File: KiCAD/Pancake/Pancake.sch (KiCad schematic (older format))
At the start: 12 parts, among them J1 Conn_01x08_Male, J2 Conn_01x08_Male, J3 Conn_01x08_Male, J4 Conn_01x10_Male, J5 Conn_01x08_Male, J6 Conn_01x08_Male

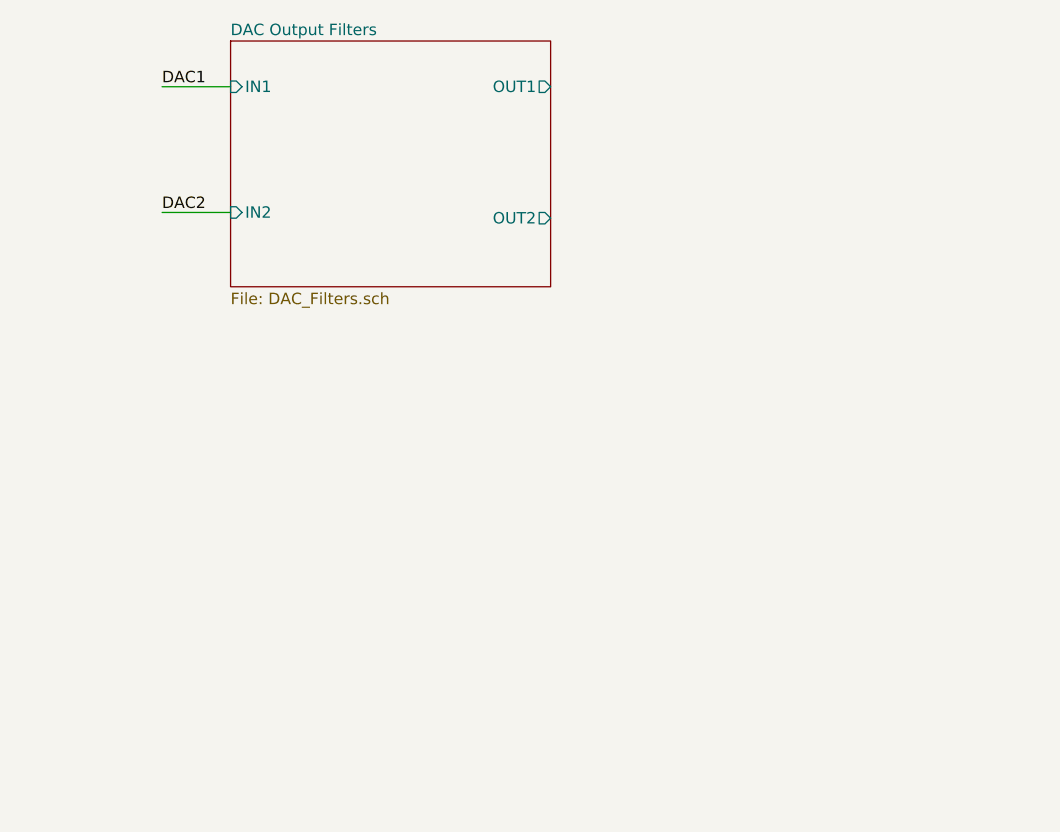
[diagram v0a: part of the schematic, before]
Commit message: All input filters/attenuators modeled and tested in ltspice
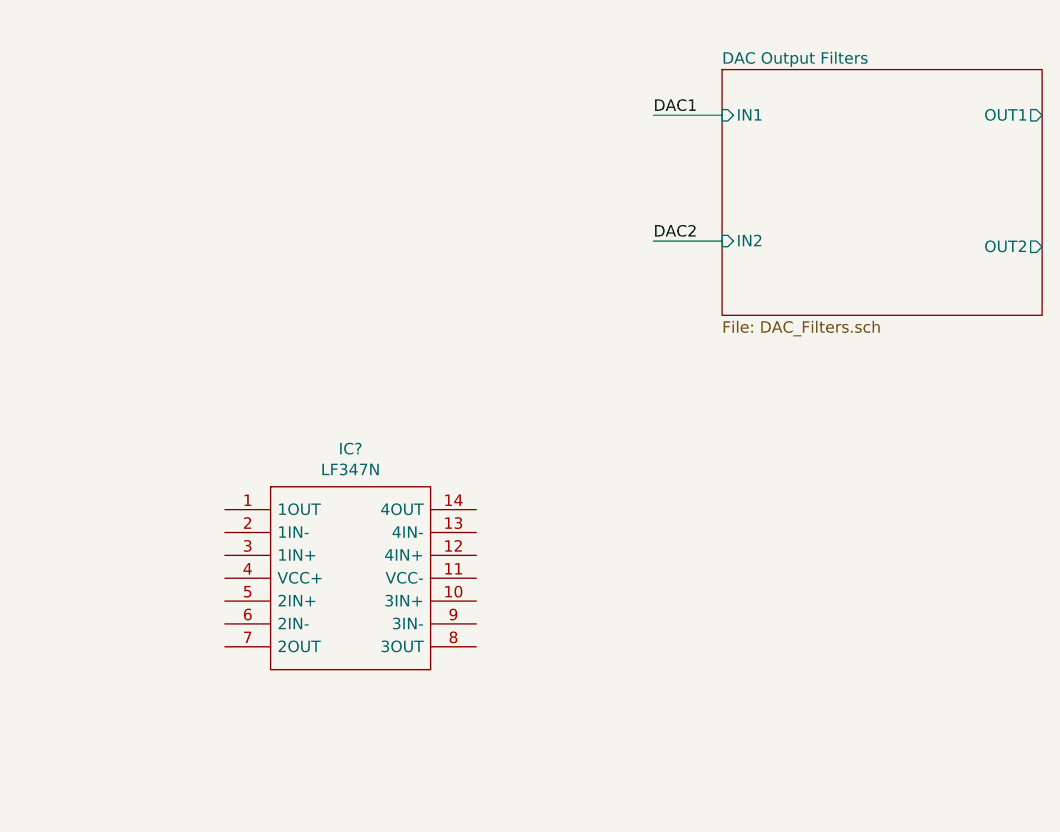
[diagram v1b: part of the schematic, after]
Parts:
- added IC?: LF347N, DIP794W56P254L1905H533Q14N, symbol SamacSys_Parts:LF347N
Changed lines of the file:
@@
 D13
 $Sheet
-S 3950 1075 1400 1075
+S 6100 1200 1400 1075
 U 61024B6A
 F0 "DAC Output Filters" 50
 F1 "DAC_Filters.sch" 50
-F2 "IN1" I L 3950 1275 50
-F3 "IN2" I L 3950 1825 50
-F4 "OUT1" O R 5350 1275 50
-F5 "OUT2" O R 5350 1850 50
+F2 "IN1" I L 6100 1400 50
+F3 "IN2" I L 6100 1950 50
+F4 "OUT1" O R 7500 1400 50
+F5 "OUT2" O R 7500 1975 50
 $EndSheet
-Text Label 3650 1275 0    50   ~ 0
+Text Label 5800 1400 0    50   ~ 0
 DAC1
-Text Label 3650 1825 0    50   ~ 0
+Text Label 5800 1950 0    50   ~ 0
 DAC2
 Wire Wire Line
-	3650 1825 3950 1825
-Wire Wire Line
-	3650 1275 3950 1275
+	5800 1950 6100 1950
+Wire Wire Line
+	5800 1400 6100 1400
 $Comp
 L SamacSys_Parts:UA7808CKTTR IC?
@@
 	5025 6275 4550 6275
 Connection ~ 4550 6275
+$Comp
+L SamacSys_Parts:LF347N IC?
+U 1 1 612701DD
+P 3925 3125
+F 0 "IC?" H 4475 3390 50  0000 C CNN
+F 1 "LF347N" H 4475 3299 50  0000 C CNN
+F 2 "DIP794W56P254L1905H533Q14N" H 4875 3225 50  0001 L CNN
+F 3 "http://www.ti.com/lit/ds/symlink/lf347-n.pdf" H 4875 3125 50  0001 L CNN
+F 4 "Quad General-Purpose JFET-input Operational Amplifier" H 4875 3025 50  0001 L CNN "Description"
+F 5 "5.334" H 4875 2925 50  0001 L CNN "Height"
+F 6 "Texas Instruments" H 4875 2825 50  0001 L CNN "Manufacturer_Name"
+F 7 "LF347N" H 4875 2725 50  0001 L CNN "Manufacturer_Part_Number"
+F 8 "595-LF347N" H 4875 2625 50  0001 L CNN "Mouser Part Number"
+F 9 "https://www.mouser.co.uk/ProductDetail/Texas-Instruments/LF347N?qs=DcvZ7Fltd5zOlQRQ%252BiS7vA%3D%3D" H 4875 2525 50  0001 L CNN "Mouser Price/Stock"
+F 10 "LF347N" H 4875 2425 50  0001 L CNN "Arrow Part Number"
+F 11 "https://www.arrow.com/en/products/lf347n/texas-instruments" H 4875 2325 50  0001 L CNN "Arrow Price/Stock"
+	1    3925 3125
+	1    0    0    -1
+$EndComp
 $EndSCHEMATC

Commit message: Extra kicad stuff
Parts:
- removed R? (x2): R, symbol Device:R
- removed U?: NEED TO ASSIGN THIS A VALUE, symbol pspice:OPAMP
- added C? (x2): 10uF, symbol Device:C
- added IC?: ICL7660SCPAZ, DIP794W56P254L958H533Q8N, symbol SamacSys_Parts:ICL7660SCPAZ
- added R? (x5): 35.6k, symbol Device:R
- added R? (x5): 29.4k, symbol Device:R
- added R? (x3): 71.5k, symbol Device:R
- added R? (x3): 26.1k, symbol Device:R
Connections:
- net labels added: -12V, ADC1, ADC2, ADC3, ADC4, ADC5, ADC6, ADC7, ADC8, AIN1, AIN2, AIN3, AIN4, AIN5, AIN6, AIN7, AIN8
- net labels removed: +4V
- wire segments 26 -> 69
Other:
- moved on the sheet: IC?

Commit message: DAC Filters and Relays
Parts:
- added C5, C6: 1mF, symbol Device:C
- added R1, R2: 143k, symbol Device:R
- added R13, R14, R27, R28: 26.1k, symbol Device:R
- added R21, R22, R7, R8: 71.5k, symbol Device:R
- added R3, R4: 22.1k, symbol Device:R
- added R? (x2): 100, symbol Device:R
- IC1: renamed from IC?; symbol SamacSys_Parts:ICL7660SCPAZ -> Pancake-rescue:ICL7660SCPAZ-SamacSys_Parts
- IC2: renamed from IC?; symbol SamacSys_Parts:UA7808CKTTR -> Pancake-rescue:UA7808CKTTR-SamacSys_Parts
- IC3: renamed from IC?; symbol SamacSys_Parts:LF347N -> Pancake-rescue:LF347N-SamacSys_Parts
- R10, R17, R5, R6, R9: renamed from R?; value 35.6k -> 53.6k
- R19: renamed from R?; value 71.5k -> 75k
- R25: renamed from R?; value 26.1k -> 25.5k
- gave numbers to parts that had none: 13
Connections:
- net labels added: 12VOut, 6VOut, 8VOut, ADC0, ADC10, ADC11, ADC9, DAC0, EmitterBypassOut, EmitterFollowerOut, GainStageOut, NegDriverOut, PosDriverOut, PreampOut, SPRKNeg, SourceFollowerOut
- net labels removed: AIN1, AIN2, AIN3, AIN4, AIN5, AIN6, AIN7, AIN8
- wire segments 69 -> 103
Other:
- moved on the sheet: C1, C4, IC3, J1, J2, J3, J5, J6, R10, R11, R12, R15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

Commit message: Re-did filters for 5% resistors
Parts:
- removed R? (x2): 100, symbol Device:R
- R1, R2: value 143k -> 91k
- R10, R17, R5, R6, R9: value 53.6k -> 68k
- R11, R12, R15, R16, R23: value 29.4k -> 39k
- R13, R14, R26, R27, R28: value 26.1k -> 33k
- R18, R20, R21, R22, R7, R8: value 71.5k -> 91k
- R19: value 75k -> 91k
- R25: value 25.5k -> 33k
- R3, R4: value 22.1k -> 33k
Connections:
- wire segments 103 -> 101
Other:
- moved on the sheet: C5, C6, R1, R2, R3, R4

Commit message: Schematic almost complete. layout still required
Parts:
- removed C1, C4: 10uF, symbol Device:C
- removed C2: 0.33uF, symbol Device:CP
- removed C3: 0.1uF, symbol Device:CP
- removed IC1: ICL7660SCPAZ, DIP794W56P254L958H533Q8N, symbol Pancake-rescue:ICL7660SCPAZ-SamacSys_Parts
- removed IC2: UA7808CKTTR, KTT-(R-PSFM-G3), symbol Pancake-rescue:UA7808CKTTR-SamacSys_Parts
- C5, C6: value 1mF -> 220nF; footprint (none) -> Resistor_THT:R_Axial_DIN0204_L3.6mm_D1.6mm_P5.08mm_Horizontal
- IC3: symbol Pancake-rescue:LF347N-SamacSys_Parts -> SamacSys_Parts:LF347N
- J1, J2, J3, J5, J6: footprint (none) -> Connector_PinHeader_2.54mm:PinHeader_1x08_P2.54mm_Vertical
- J4: footprint (none) -> Connector_PinHeader_2.54mm:PinHeader_1x10_P2.54mm_Vertical
- R1, R10, R11, R12, R13, R14, R15, R16, R17, R18, R19, R2, R20, R21, R22, R23, R25, R26, R27, R28, R3, R4, R5, R6, R7, R8, R9: footprint (none) -> Resistor_THT:R_Axial_DIN0207_L6.3mm_D2.5mm_P10.16mm_Horizontal
- R24: value 26.1k -> 33k; footprint (none) -> Resistor_THT:R_Axial_DIN0207_L6.3mm_D2.5mm_P10.16mm_Horizontal
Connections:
- net labels removed: +8V
- wire segments 101 -> 80
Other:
- moved on the sheet: C5, C6, R1, R2, R3, R4

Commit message: Ribbon cable connector, arduino layout
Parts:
- removed J4: Conn_01x10_Male, Connector_PinHeader_2.54mm:PinHeader_1x10_P2.54mm_Vertical, symbol Connector:Conn_01x10_Male
- removed J6: Conn_01x08_Male, Connector_PinHeader_2.54mm:PinHeader_1x08_P2.54mm_Vertical, symbol Connector:Conn_01x08_Male
- added J7: Conn_02x15_Top_Bottom, Connector_PinSocket_2.54mm:PinSocket_2x15_P2.54mm_Vertical, symbol Connector_Generic:Conn_02x15_Top_Bottom
- added J?: Conn_01x08_Male, Connector_PinHeader_2.54mm:PinHeader_1x08_P2.54mm_Vertical, symbol Connector:Conn_01x08_Male
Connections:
- net labels added: AuxIn, DriveHigh, DriveLow, DriveMid, GuitarIn, PresenceIn, PresenceOut, SPRKPos, ToneHigh, ToneLow, ToneMid, VolumeHigh, VolumeLow, VolumeMid
- net labels removed: A0, A1, A10, A11, A2, A3, A4, A5, A6, A7, A8, A9, D0, D1, D13, DAC0, VDD
- wire segments 80 -> 68
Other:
- note added: "Arduino Header Pins"
- moved on the sheet: C5, C6, J2, J3, J5, R1, R2, R3, R4

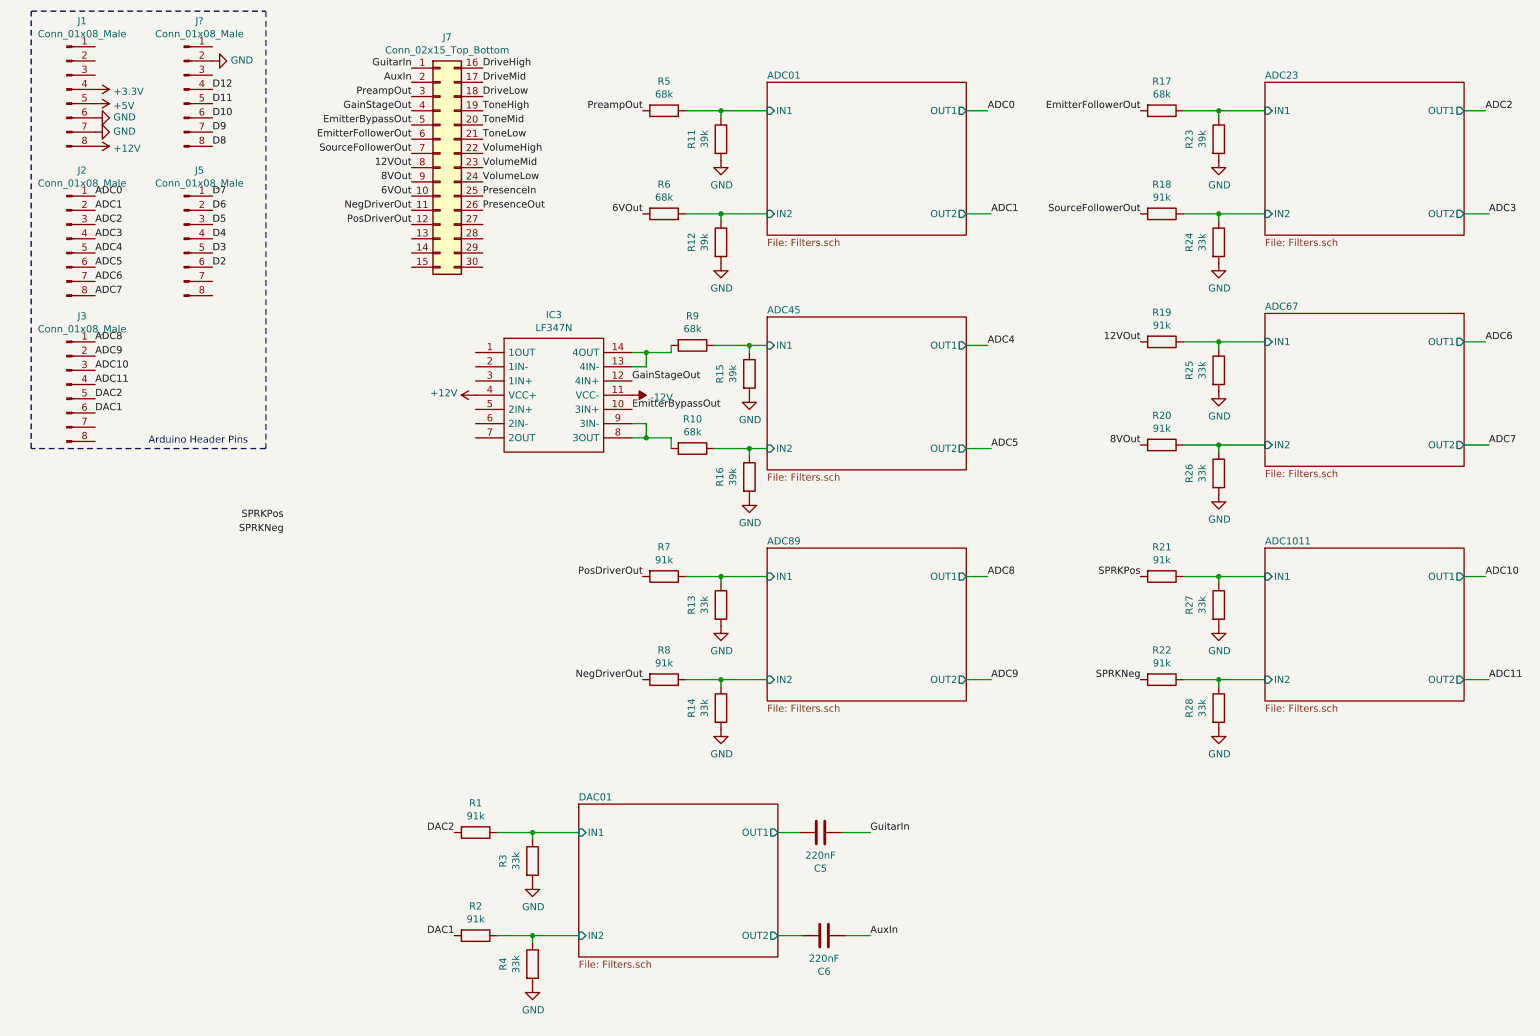
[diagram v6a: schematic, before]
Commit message: Arduino laid out
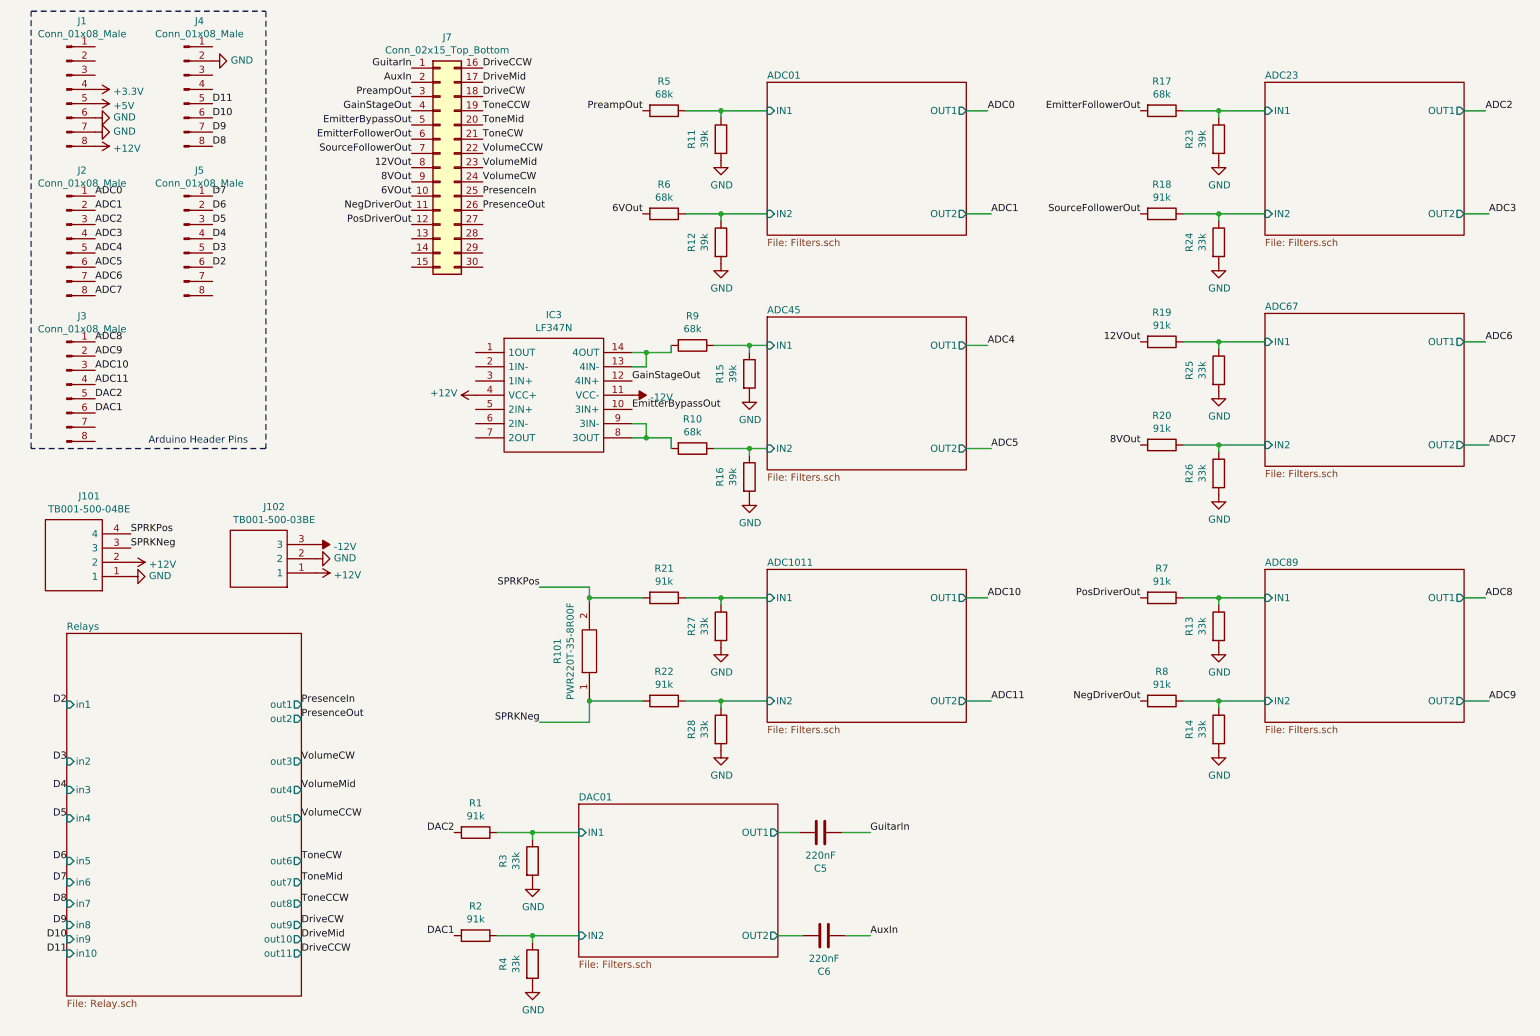
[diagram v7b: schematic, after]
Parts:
- added J101: TB001-500-04BE, TB00150004BE, symbol SamacSys_Parts:TB001-500-04BE
- added J102: TB001-500-03BE, TB00150003BE, symbol SamacSys_Parts:TB001-500-03BE
- added R101: PWR220T-35-8R00F, TO508P438X1010X1539-2P, symbol SamacSys_Parts:PWR220T-35-8R00F
- gave numbers to parts that had none: 1
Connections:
- net +12V: now also J101.2, J102.1
- net -12V: now also J102.3
- net GND: now also J101.1, J102.2
- net SPRKNeg: now also J101.3, R101.1
- net SPRKPos: now also J101.4, R101.2
- net D12: no longer names the net of J4.4 (Pin_4)
- net DriveHigh renamed DriveCCW
- net DriveLow renamed DriveCW
- net ToneHigh renamed ToneCCW
- net ToneLow renamed ToneCW
- net VolumeHigh renamed VolumeCCW
- net VolumeLow renamed VolumeCW
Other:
- moved on the sheet: R13, R14, R21, R22, R27, R28, R7, R8

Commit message: Models
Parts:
- C5, C6: footprint Resistor_THT:R_Axial_DIN0204_L3.6mm_D1.6mm_P5.08mm_Horizontal -> Capacitor_THT:C_Disc_D4.3mm_W1.9mm_P5.00mm
- J101: symbol SamacSys_Parts:TB001-500-04BE -> Pancake-rescue:TB001-500-04BE-SamacSys_Parts
- J102: symbol SamacSys_Parts:TB001-500-03BE -> Pancake-rescue:TB001-500-03BE-SamacSys_Parts
- R101: symbol SamacSys_Parts:PWR220T-35-8R00F -> Pancake-rescue:PWR220T-35-8R00F-SamacSys_Parts
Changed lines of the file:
@@
 F 0 "C5" V 5898 6350 50  0000 C CNN
 F 1 "220nF" V 5989 6350 50  0000 C CNN
-F 2 "Resistor_THT:R_Axial_DIN0204_L3.6mm_D1.6mm_P5.08mm_Horizontal" H 6188 6200 50  0001 C CNN
+F 2 "Capacitor_THT:C_Disc_D4.3mm_W1.9mm_P5.00mm" H 6188 6200 50  0001 C CNN
 F 3 "~" H 6150 6350 50  0001 C CNN
 	1    6150 6350
@@
 F 0 "C6" V 5923 7075 50  0000 C CNN
 F 1 "220nF" V 6014 7075 50  0000 C CNN
-F 2 "Resistor_THT:R_Axial_DIN0204_L3.6mm_D1.6mm_P5.08mm_Horizontal" H 6213 6925 50  0001 C CNN
+F 2 "Capacitor_THT:C_Disc_D4.3mm_W1.9mm_P5.00mm" H 6213 6925 50  0001 C CNN
 F 3 "~" H 6175 7075 50  0001 C CNN
 	1    6175 7075
@@
 PresenceOut
 $Comp
-L SamacSys_Parts:PWR220T-35-8R00F R101
+L Pancake-rescue:PWR220T-35-8R00F-SamacSys_Parts R101
 U 1 1 614C8890
 P 4525 5425
@@
 $EndComp
 $Comp
-L SamacSys_Parts:TB001-500-04BE J101
+L Pancake-rescue:TB001-500-04BE-SamacSys_Parts J101
 U 1 1 6131A74D
 P 1300 4550
@@
 Connection ~ 4525 5425
 $Comp
-L SamacSys_Parts:TB001-500-03BE J102
+L Pancake-rescue:TB001-500-03BE-SamacSys_Parts J102
 U 1 1 6151F148
 P 2600 4525
